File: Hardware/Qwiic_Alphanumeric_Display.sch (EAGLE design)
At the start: 33 parts, among them J4 Vertical Qwiic Connector, J5 Vertical Qwiic Connector, U2 XC9140

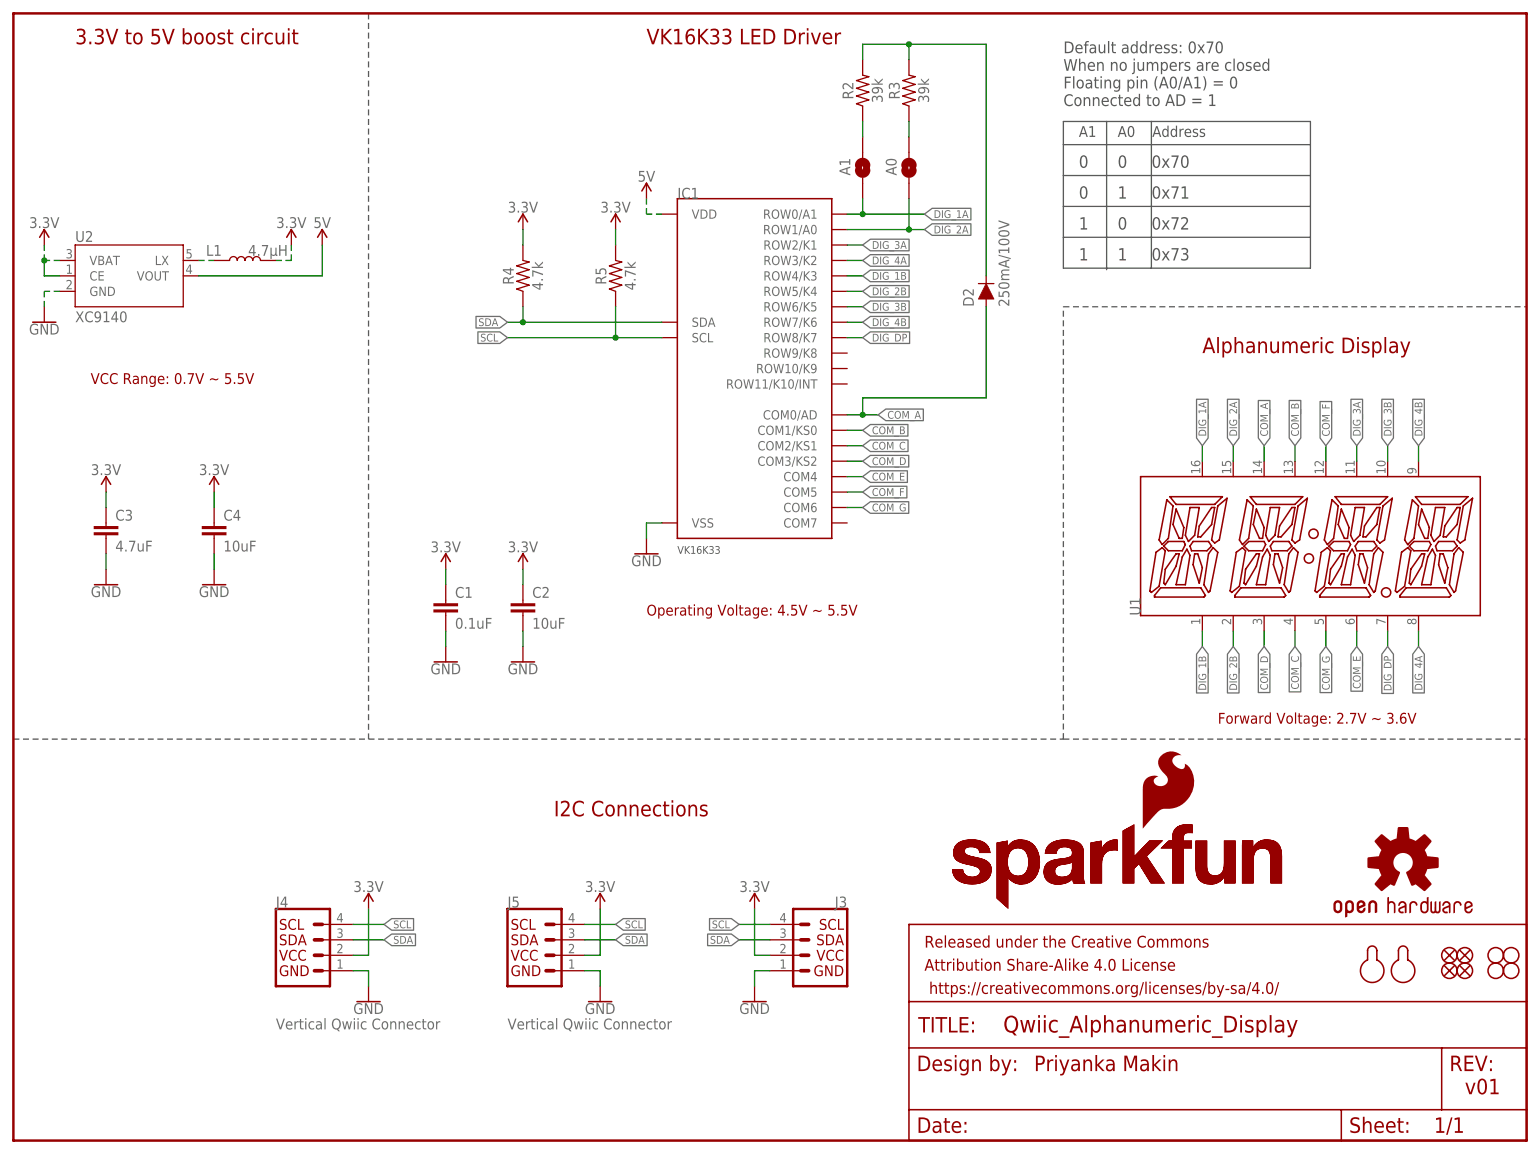
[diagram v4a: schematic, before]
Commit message: Pete's design updates
* Update address table with "open" and "closed"
* Move address resistors and jumpers
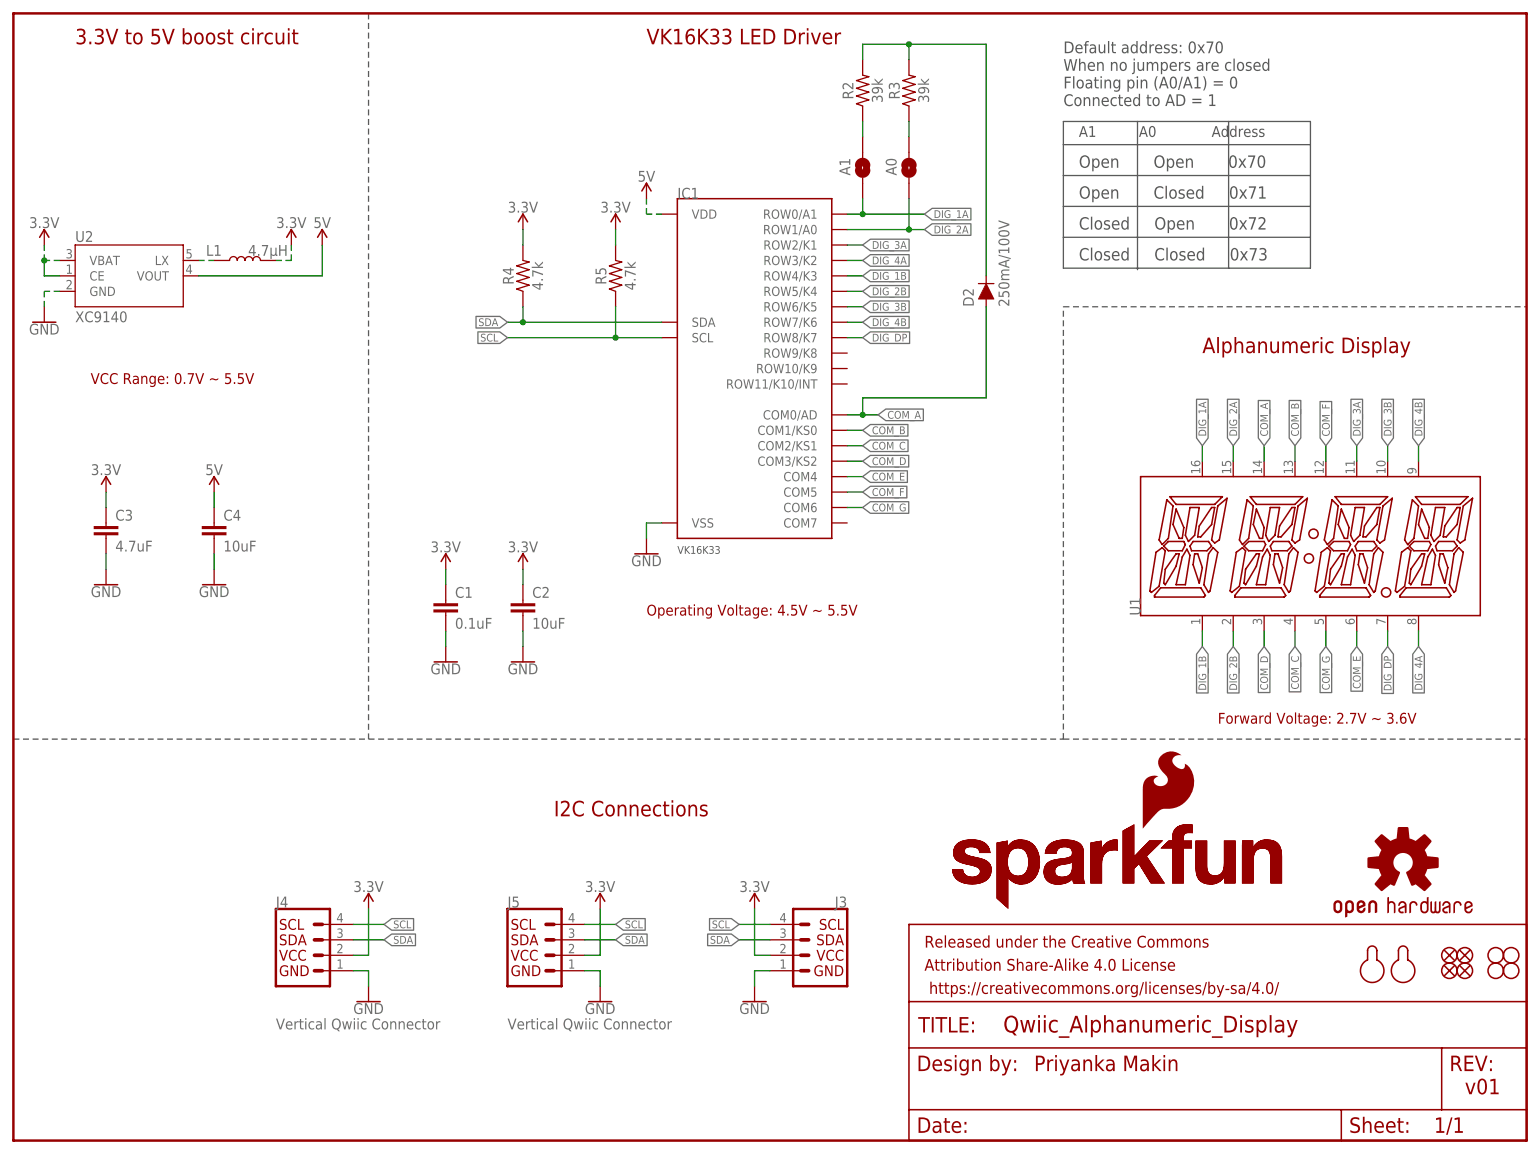
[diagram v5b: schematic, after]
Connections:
- net 3.3V: no longer C4.1
- net 5V: now also C4.1
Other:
- note added: "Closed Closed 0x73"
- note added: "Closed Open 0x72"
- note added: "Open Closed 0x71"
- note added: "Open Open 0x70"
- note removed: "0 0 0x70"
- note removed: "0 1 0x71"
- note removed: "1 0 0x72"
- note removed: "1 1 0x73"
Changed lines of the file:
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@@
 <part name="GND10" library="SparkFun-PowerSymbols" deviceset="GND" device=""/>
 <part name="SUPPLY10" library="SparkFun-PowerSymbols" deviceset="3.3V" device=""/>
-<part name="SUPPLY11" library="SparkFun-PowerSymbols" deviceset="3.3V" device=""/>
 <part name="L1" library="SparkFun-Coils" deviceset="INDUCTOR" device="-CDRH-4.7UH" value="4.7µH"/>
 <part name="SUPPLY12" library="SparkFun-PowerSymbols" deviceset="3.3V" device=""/>
@@
 <part name="SUPPLY1" library="SparkFun-PowerSymbols" deviceset="3.3V" device=""/>
 <part name="SUPPLY9" library="SparkFun-PowerSymbols" deviceset="3.3V" device=""/>
+<part name="SUPPLY11" library="SparkFun-PowerSymbols" deviceset="5V" device=""/>
 </parts>
 <sheets>
@@
 <wire x1="0" y1="66.04" x2="58.42" y2="66.04" width="0.2032" layer="97" style="longdash"/>
 <text x="88.9" y="53.34" size="2.54" layer="94" font="vector">I2C Connections</text>
-<text x="175.26" y="165.1" size="1.778" layer="97" font="vector">A1     A0    Address</text>
-<text x="175.26" y="160.02" size="2.032" layer="97" font="vector">0      0     0x70</text>
-<text x="175.26" y="154.94" size="2.032" layer="97" font="vector">0      1     0x71</text>
-<text x="175.26" y="149.86" size="2.032" layer="97" font="vector">1      0     0x72</text>
-<text x="175.26" y="144.78" size="2.032" layer="97" font="vector">1      1     0x73</text>
+<text x="175.26" y="165.1" size="1.778" layer="97" font="vector">A1          A0             Address</text>
 <wire x1="58.42" y1="66.04" x2="172.72" y2="66.04" width="0.2032" layer="97" style="longdash"/>
 <wire x1="172.72" y1="66.04" x2="248.92" y2="66.04" width="0.2032" layer="97" style="longdash"/>
@@
 <wire x1="172.72" y1="153.67" x2="172.72" y2="148.59" width="0.2032" layer="97"/>
 <wire x1="172.72" y1="148.59" x2="172.72" y2="143.51" width="0.2032" layer="97"/>
-<wire x1="172.72" y1="167.64" x2="179.832" y2="167.64" width="0.2032" layer="97"/>
-<wire x1="179.832" y1="167.64" x2="187.198" y2="167.64" width="0.2032" layer="97"/>
-<wire x1="187.198" y1="167.64" x2="213.36" y2="167.64" width="0.2032" layer="97"/>
+<wire x1="172.72" y1="167.64" x2="184.912" y2="167.64" width="0.2032" layer="97"/>
+<wire x1="184.912" y1="167.64" x2="199.898" y2="167.64" width="0.2032" layer="97"/>
+<wire x1="199.898" y1="167.64" x2="213.36" y2="167.64" width="0.2032" layer="97"/>
 <wire x1="213.36" y1="167.64" x2="213.36" y2="163.83" width="0.2032" layer="97"/>
 <wire x1="213.36" y1="163.83" x2="213.36" y2="158.75" width="0.2032" layer="97"/>
@@
 <wire x1="172.72" y1="153.67" x2="213.36" y2="153.67" width="0.2032" layer="97"/>
 <wire x1="172.72" y1="148.59" x2="213.36" y2="148.59" width="0.2032" layer="97"/>
-<wire x1="172.72" y1="143.51" x2="187.198" y2="143.51" width="0.2032" layer="97"/>
+<wire x1="172.72" y1="143.51" x2="199.898" y2="143.51" width="0.2032" layer="97"/>
 <text x="172.72" y="170.18" size="1.9304" layer="97" font="vector">Default address: 0x70
 When no jumpers are closed
 Floating pin (A0/A1) = 0
 Connected to AD = 1</text>
-<wire x1="187.198" y1="143.51" x2="213.36" y2="143.51" width="0.2032" layer="97"/>
-<wire x1="179.832" y1="167.64" x2="179.832" y2="143.256" width="0.2032" layer="97"/>
-<wire x1="187.198" y1="167.64" x2="187.198" y2="143.51" width="0.2032" layer="97"/>
+<wire x1="199.898" y1="143.51" x2="213.36" y2="143.51" width="0.2032" layer="97"/>
+<wire x1="184.912" y1="167.64" x2="184.912" y2="143.256" width="0.2032" layer="97"/>
+<wire x1="199.898" y1="167.64" x2="199.898" y2="143.51" width="0.2032" layer="97"/>
 <text x="238.76" y="7.62" size="2.54" layer="94" font="vector">v01</text>
 <wire x1="172.72" y1="66.04" x2="172.72" y2="137.16" width="0.2032" layer="97" style="longdash"/>
@@
 <text x="104.14" y="86.36" size="1.778" layer="94" font="vector">Operating Voltage: 4.5V ~ 5.5V</text>
 <text x="198.12" y="68.58" size="1.778" layer="94" font="vector">Forward Voltage: 2.7V ~ 3.6V</text>
+<text x="175.26" y="154.94" size="2.032" layer="97" font="vector">Open       Closed     0x71</text>
+<text x="175.26" y="160.02" size="2.032" layer="97" font="vector">Open       Open       0x70</text>
+<text x="175.26" y="149.86" size="2.032" layer="97" font="vector">Closed     Open       0x72</text>
+<text x="175.26" y="144.78" size="2.032" layer="97" font="vector">Closed     Closed     0x73</text>
 </plain>
 <instances>
@@
 <attribute name="VALUE" x="15.24" y="109.474" size="1.778" layer="96" font="vector" align="bottom-center"/>
 </instance>
-<instance part="SUPPLY11" gate="G$1" x="33.02" y="106.68" smashed="yes">
-<attribute name="VALUE" x="33.02" y="109.474" size="1.778" layer="96" font="vector" align="bottom-center"/>
-</instance>
 <instance part="L1" gate="G$1" x="38.1" y="144.78" smashed="yes" rot="R90">
 <attribute name="NAME" x="34.29" y="147.32" size="1.778" layer="95" font="vector" rot="R180"/>
@@
 <attribute name="VALUE" x="99.06" y="152.654" size="1.778" layer="96" align="bottom-center"/>
 </instance>
+<instance part="SUPPLY11" gate="G$1" x="33.02" y="106.68" smashed="yes">
+<attribute name="VALUE" x="33.02" y="109.474" size="1.778" layer="96" align="bottom-center"/>
+</instance>
 </instances>
 <busses>
@@
 <pinref part="SUPPLY10" gate="G$1" pin="3.3V"/>
 <wire x1="15.24" y1="106.68" x2="15.24" y2="104.14" width="0.1524" layer="91"/>
-</segment>
-<segment>
-<pinref part="C4" gate="G$1" pin="1"/>
-<pinref part="SUPPLY11" gate="G$1" pin="3.3V"/>
-<wire x1="33.02" y1="106.68" x2="33.02" y2="104.14" width="0.1524" layer="91"/>
 </segment>
 <segment>
@@
 <wire x1="50.8" y1="142.24" x2="50.8" y2="147.32" width="0.1524" layer="91"/>
 </segment>
-</net>
+<segment>
+<pinref part="C4" gate="G$1" pin="1"/>
+<pinref part="SUPPLY11" gate="G$1" pin="5V"/>
+<wire x1="33.02" y1="106.68" x2="33.02" y2="104.14" width="0.1524" layer="91"/>
+</segment>
+</net>

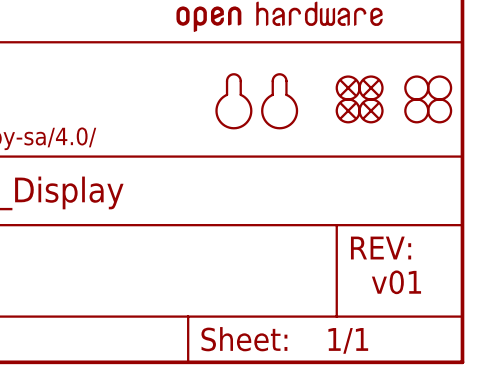
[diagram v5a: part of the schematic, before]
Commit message: Pete's updates
* Some silk updates: default address and address jumper labels
* Bump version number v01 --> v10
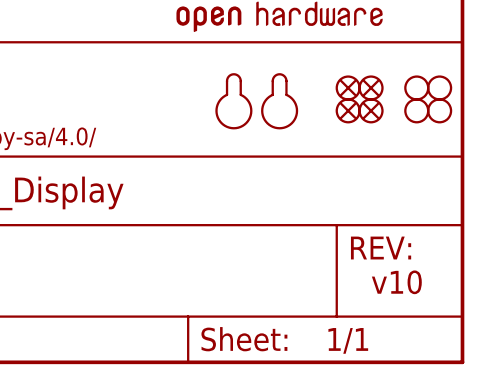
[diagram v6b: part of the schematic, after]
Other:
- note added: "v10"
- note removed: "v01"
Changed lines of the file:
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@@
 <?xml version="1.0" encoding="utf-8"?>
 <!DOCTYPE eagle SYSTEM "eagle.dtd">
-<eagle version="9.5.2">
+<eagle version="9.4.2">
 <drawing>
 <settings>
-<setting alwaysvectorfont="no"/>
+<setting alwaysvectorfont="yes"/>
 <setting verticaltext="up"/>
 </settings>
@@
 <wire x1="184.912" y1="167.64" x2="184.912" y2="143.256" width="0.2032" layer="97"/>
 <wire x1="199.898" y1="167.64" x2="199.898" y2="143.51" width="0.2032" layer="97"/>
-<text x="238.76" y="7.62" size="2.54" layer="94" font="vector">v01</text>
+<text x="238.76" y="7.62" size="2.54" layer="94" font="vector">v10</text>
 <wire x1="172.72" y1="66.04" x2="172.72" y2="137.16" width="0.2032" layer="97" style="longdash"/>
 <wire x1="172.72" y1="137.16" x2="248.92" y2="137.16" width="0.2032" layer="97" style="longdash"/>
